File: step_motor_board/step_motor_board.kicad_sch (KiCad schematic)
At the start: 39 parts, among them J1 Prog (PinHeader_2x03_P2.54mm), J7 DebugUSART (PinHeader_01x03_P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, J8 Debug GPIO (PinHeader_01x02_P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, Q4 DTC114ECA (SOT-23), Q5 DTC114ECA (SOT-23), U1 ADM3485EARZ-REEL (SOIC-8), U3 STM32G070RBTx (LQFP-64), U5 AM1SS-2403SJZ, U9 PAI141M30 (SOIC-16)

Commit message: DC, contr, mb, step v2
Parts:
- removed J1: Prog (PinHeader_2x03_P2.54mm), Connector_PinHeader_2.54mm:PinHeader_2x03_P2.54mm_Vertical, symbol Connector_Generic:Conn_02x03_Odd_Even
- removed J7: DebugUSART (PinHeader_01x03_P2.54mm), Connector_PinHeader_2.54mm:PinHeader_1x03_P2.54mm_Vertical, symbol Connector:Conn_01x03_Pin
- removed J8: Debug GPIO (PinHeader_01x02_P2.54mm), Connector_PinHeader_2.54mm:PinHeader_1x02_P2.54mm_Vertical, symbol Connector:Conn_01x02_Pin
- added C42, C43: 20pF 50V 0603, Capacitor_SMD:C_0603_1608Metric, symbol Device:C
- added J1: PLL-10 (Prog), Connector_PinHeader_1.27mm:PinHeader_1x10_P1.27mm_Vertical, symbol Connector:Conn_01x10_Pin
- added TP20 (x11): TestPoint, PCM_4ms_TestPoint:TestPoint_D1, symbol Connector:TestPoint
- added Y1: Crystal_3225 8MHz, PCM_Crystal_AKL:Crystal_SMD_3225-4Pin_3.2x2.5mm, symbol Device:Crystal_GND24
- C14: value 47uF 63V D10,5 -> 47uF 63V D6,3 H11
- C3, C6, C7: value 0,1uF 50V 0805 -> 0,1uF 100V 0603; footprint PCM_Resistor_SMD_AKL:R_0805_2012Metric_Pad1.20x1.40mm_HandSolder -> Capacitor_SMD:C_0603_1608Metric_Pad1.08x0.95mm_HandSolder
- C4: footprint PCM_Resistor_SMD_AKL:R_0805_2012Metric_Pad1.20x1.40mm_HandSolder -> PCM_Capacitor_SMD_AKL:C_0805_2012Metric_Pad1.18x1.45mm_HandSolder
- C5, C8, C9: value 0,1uF 100V 0805 -> 0,1uF 100V 0603; footprint PCM_Capacitor_SMD_AKL:C_0805_2012Metric_Pad1.18x1.45mm_HandSolder -> Capacitor_SMD:C_0603_1608Metric_Pad1.08x0.95mm_HandSolder
- U9: value PAI141M30 (SOIC-16) -> Pai141M30 (SOIC-16)
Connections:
- net +24V: now also TP20.1
- net +3.3VRS485: now also TP20.1
- net +3V3: now also J1.1 (Pin_1)
- net GND1: now also TP20.1
- net GNDA: now also TP20.1
- net GNDD: now also C42.2, C43.2, J1.6 (Pin_6), TP20.1, Y1.2, Y1.4
- net GPIO1: now also J1.9 (Pin_9)
- net GPIO2: now also J1.10 (Pin_10)
- net NRST: now also J1.5 (Pin_5)
- net SWCLK: now also J1.3 (Pin_3)
- net SWDIO: now also J1.4 (Pin_4)
- net UART_RX: now also J1.8 (Pin_8)
- net UART_TX: now also J1.7 (Pin_7)
- net at R3.1, RS1.3 (Pin_3), RS1.8 (Pin_8)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: now also TP20.1
- net OSC_IN: now reaches U3.10 (PF0)
- net OSC_IN: now also C42.1, Y1.1
- net OSC_OUT: now reaches U3.11 (PF1)
- net OSC_OUT: now also C43.1, Y1.3
- net at R6.2, RS1.4 (Pin_4), RS1.7 (Pin_7)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: now also TP20.1
- net at R8.2, U1.2 (~{RE}), U1.3 (DE)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: now also TP20.1
- net at R1.1, U1.1 (RO), U9.11 (VID): now also TP20.1
- net at U1.4 (DI), U9.13 (VOB): now also TP20.1
- net at C12.1, L1.2, U5.2 (IN+): now also TP20.1
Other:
- moved on the sheet: C7, R1

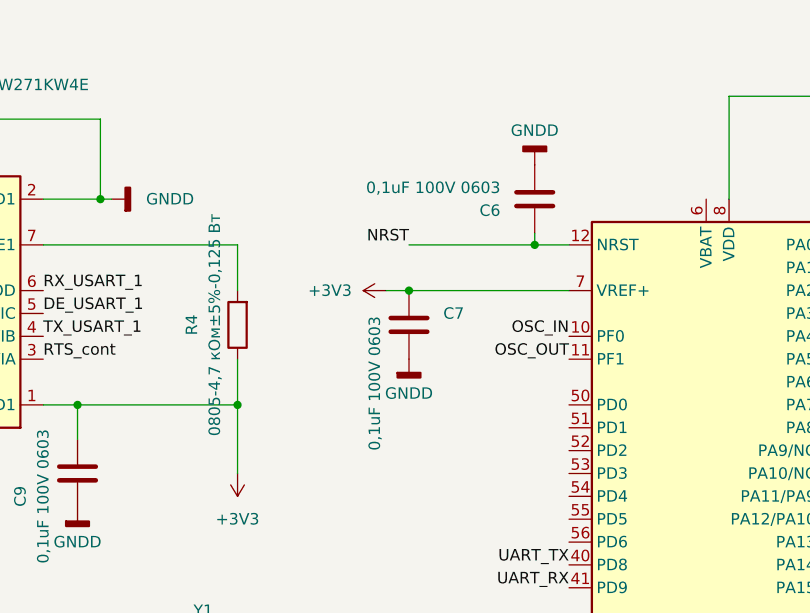
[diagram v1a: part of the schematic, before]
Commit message: Step  установлена бусинка
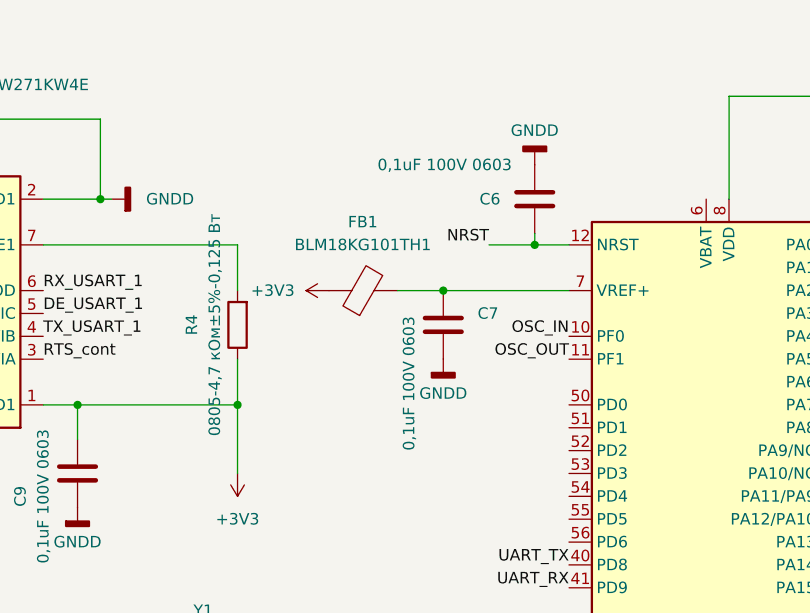
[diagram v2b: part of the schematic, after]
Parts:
- added FB1: BLM18KG101TH1, Inductor_SMD:L_0603_1608Metric, symbol Device:FerriteBead
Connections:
- net +3V3: now also FB1.1; no longer C7.1, U3.7 (VREF+)
- new net: C7.1, FB1.2, U3.7 (VREF+)
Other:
- moved on the sheet: C7

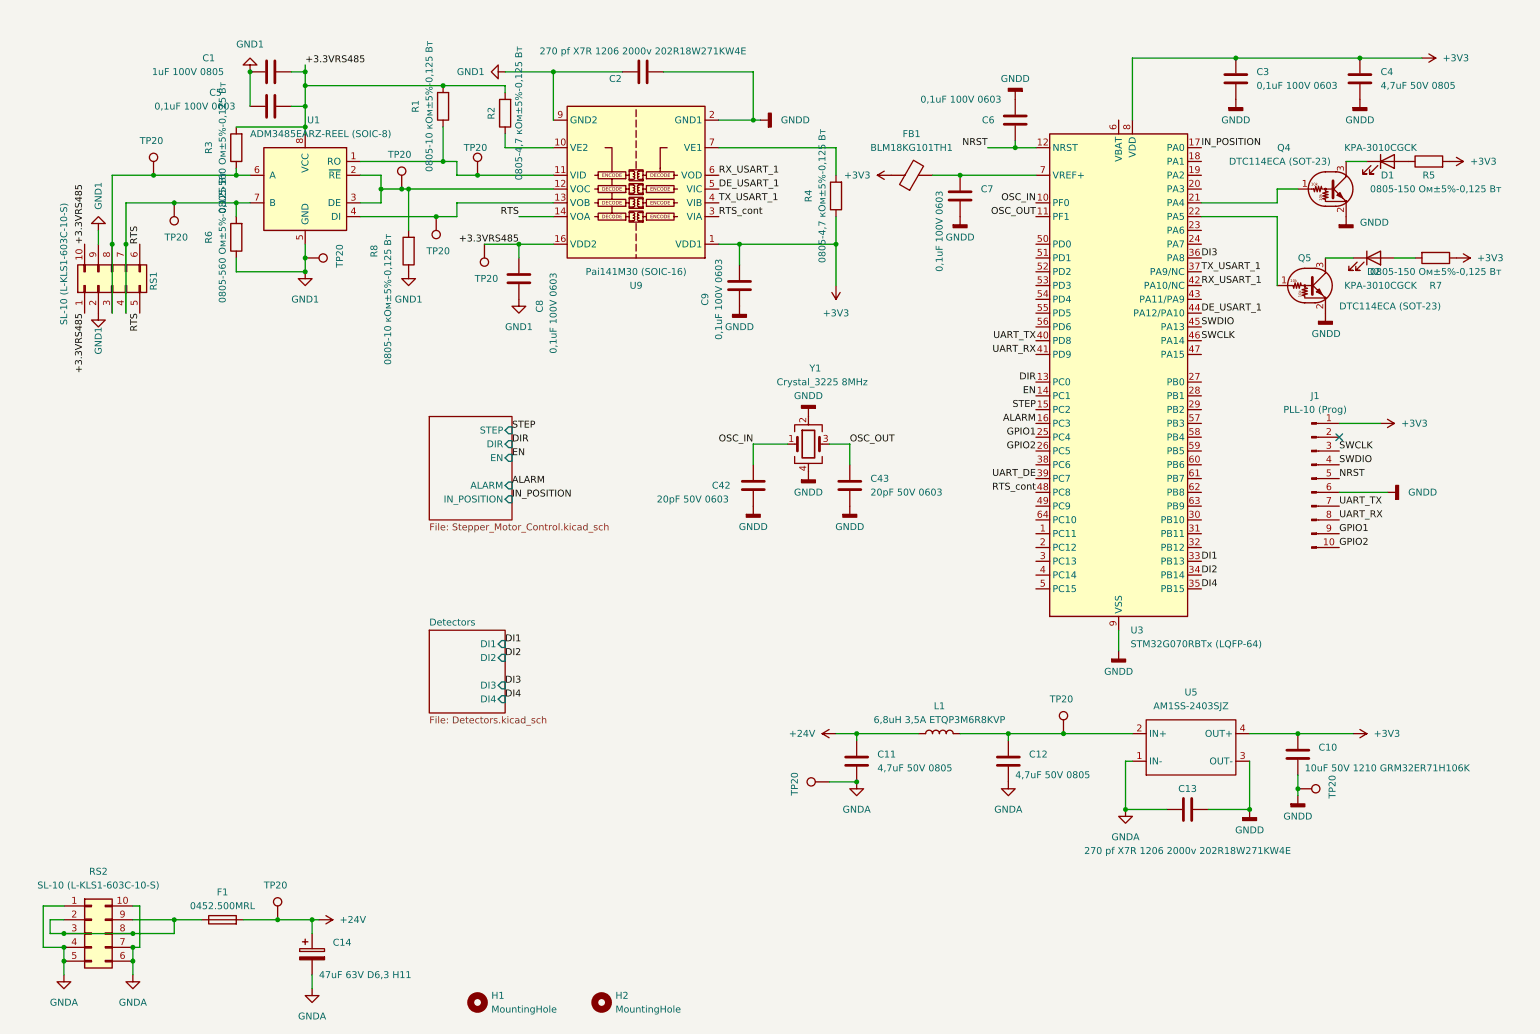
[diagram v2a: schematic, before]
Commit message: all замменил резисторы failsafe в плате контроллера и обрал из перечня во всех остальных
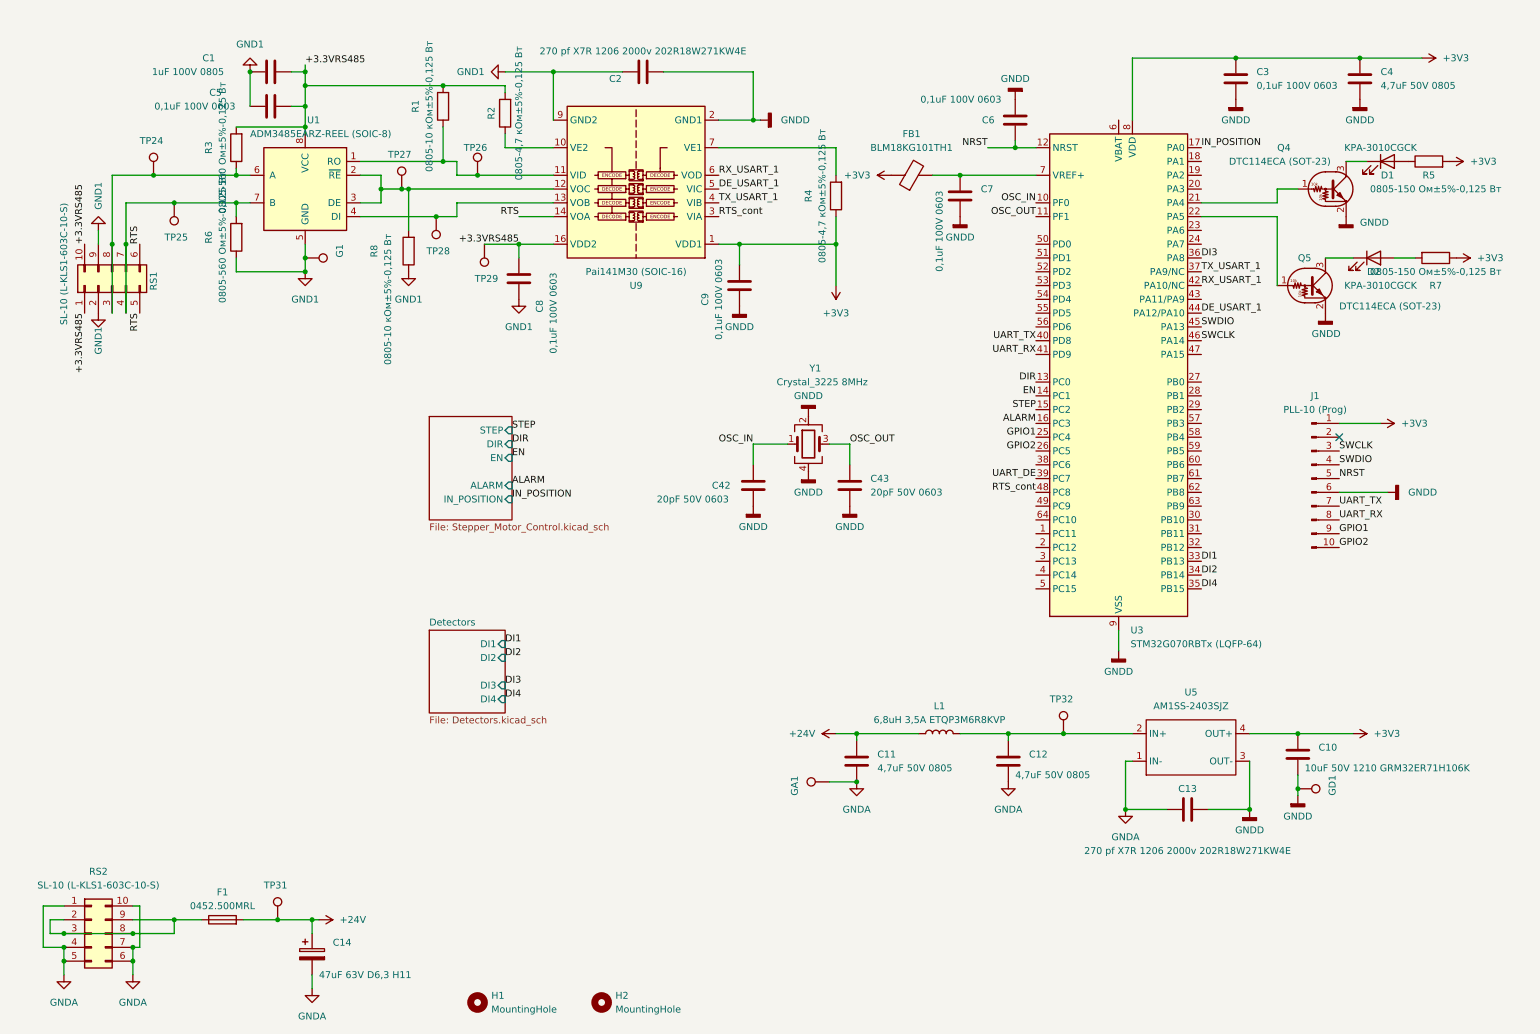
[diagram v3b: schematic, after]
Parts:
- C1, C11, C12, C4: footprint PCM_Capacitor_SMD_AKL:C_0805_2012Metric_Pad1.18x1.45mm_HandSolder -> Capacitor_SMD:C_0805_2012Metric
- C10: footprint PCM_Capacitor_SMD_AKL:C_1210_3225Metric_Pad1.42x2.65mm_HandSolder -> Capacitor_SMD:C_1210_3225Metric
- C13, C2: footprint PCM_Capacitor_SMD_Handsoldering_AKL:C_1210_3225Metric_Pad1.42x2.65mm -> Capacitor_SMD:C_1210_3225Metric
- C14: footprint PCM_Capacitor_THT_AKL:CP_Radial_D6.3mm_P2.50mm -> Capacitor_THT:CP_Radial_D6.3mm_P2.50mm
- C3, C5, C6, C7, C8, C9: footprint Capacitor_SMD:C_0603_1608Metric_Pad1.08x0.95mm_HandSolder -> Capacitor_SMD:C_0603_1608Metric
- F1: footprint PCM_Fuse_Handsoldering_AKL:Fuse_Littelfuse-NANO2-451_453 -> Fuse:Fuse_Littelfuse-NANO2-451_453
- G1, GA1, GD1, TP24, TP25, TP26, TP27, TP28, TP29, TP31, TP32: renamed from TP20; footprint PCM_4ms_TestPoint:TestPoint_D1 -> TestPoint:TestPoint_Pad_D1.0mm
- L1: footprint PCM_Inductor_SMD_Handsoldering_AKL:L_Bourns-SRN6028 -> Inductor_SMD:L_Bourns-SRN6028
- R1, R2, R4, R5, R7, R8: footprint PCM_4ms_Resistor:R_0805_2012Metric -> Resistor_SMD:R_0805_2012Metric
- R3, R6: footprint PCM_4ms_Resistor:R_0805_2012Metric -> Resistor_SMD:R_0805_2012Metric; now left out of the parts list
- Y1: footprint PCM_Crystal_AKL:Crystal_SMD_3225-4Pin_3.2x2.5mm -> Crystal:Crystal_SMD_3225-4Pin_3.2x2.5mm

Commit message: update schemas
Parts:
- C13, C2: value 270 pf X7R 1206 2000v 202R18W271KW4E -> 270 pf X7R 1206 2000v (202R18W271KW4E)
- F1: value 0452.500MRL -> 0451.500MRL
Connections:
- net DI1: now also U3.34 (PB14); no longer U3.33 (PB13)
- net DI2: now also U3.33 (PB13); no longer U3.34 (PB14)
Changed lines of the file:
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@@
 (kicad_sch
-	(version 20231120)
+	(version 20250114)
 	(generator "eeschema")
-	(generator_version "8.0")
+	(generator_version "9.0")
 	(paper "A4")
 	(junction
@@
 	(label "+3.3VRS485"
 		(at 22.86 50.8 90)
-		(fields_autoplaced yes)
 		(effects
 			(font
@@
 	(label "NRST"
 		(at 189.23 33.02 180)
-		(fields_autoplaced yes)
 		(effects
 			(font
@@
 		)
 	)
-	(label "DI1"
+	(label "DI2"
 		(at 228.6 109.22 0)
-		(fields_autoplaced yes)
 		(effects
 			(font
@@
 	(label "RTS_cont"
 		(at 139.7 45.72 0)
-		(fields_autoplaced yes)
 		(effects
 			(font
@@
 	(label "UART_TX"
 		(at 254 99.06 0)
-		(fields_autoplaced yes)
 		(effects
 			(font
@@
 	(label "UART_RX"
 		(at 254 101.6 0)
-		(fields_autoplaced yes)
 		(effects
 			(font
@@
 	(label "STEP"
 		(at 198.12 81.28 180)
-		(fields_autoplaced yes)
 		(effects
 			(font
@@
 	(label "IN_POSITION"
 		(at 101.6 97.79 0)
-		(fields_autoplaced yes)
 		(effects
 			(font
@@
 	(label "UART_TX"
 		(at 198.12 68.58 180)
-		(fields_autoplaced yes)
 		(effects
 			(font
@@
 	(label "RX_USART_1"
 		(at 228.6 58.42 0)
-		(fields_autoplaced yes)
 		(effects
 			(font
@@
 	(label "DIR"
 		(at 198.12 76.2 180)
-		(fields_autoplaced yes)
 		(effects
 			(font
@@
 	(label "UART_RX"
 		(at 198.12 71.12 180)
-		(fields_autoplaced yes)
 		(effects
 			(font
@@
 	(label "GPIO2"
 		(at 198.12 88.9 180)
-		(fields_autoplaced yes)
 		(effects
 			(font
@@
 	(label "ALARM"
 		(at 101.6 95.25 0)
-		(fields_autoplaced yes)
 		(effects
 			(font
@@
 	(label "UART_DE"
 		(at 198.12 93.98 180)
-		(fields_autoplaced yes)
 		(effects
 			(font
@@
 	(label "DE_USART_1"
 		(at 228.6 63.5 0)
-		(fields_autoplaced yes)
 		(effects
 			(font
@@
 	(label "OSC_OUT"
 		(at 163.83 87.63 0)
-		(fields_autoplaced yes)
 		(effects
 			(font
@@
 	(label "OSC_IN"
 		(at 198.12 43.18 180)
-		(fields_autoplaced yes)
 		(effects
 			(font
@@
 	(label "ALARM"
 		(at 198.12 83.82 180)
-		(fields_autoplaced yes)
 		(effects
 			(font
@@
 	(label "RTS_cont"
 		(at 198.12 96.52 180)
-		(fields_autoplaced yes)
 		(effects
 			(font
@@
 	(label "RTS"
 		(at 33.02 63.5 270)
-		(fields_autoplaced yes)
 		(effects
 			(font
@@
 	(label "RTS"
 		(at 33.02 50.8 90)
-		(fields_autoplaced yes)
 		(effects
 			(font
@@
 	(label "DIR"
 		(at 101.6 87.63 0)
-		(fields_autoplaced yes)
 		(effects
 			(font
@@
 	(label "GPIO1"
 		(at 254 104.14 0)
-		(fields_autoplaced yes)
 		(effects
 			(font
@@
 	(label "SWDIO"
 		(at 228.6 66.04 0)
-		(fields_autoplaced yes)
 		(effects
 			(font
@@
 	(label "SWCLK"
 		(at 254 88.9 0)
-		(fields_autoplaced yes)
 		(effects
 			(font
@@
 	(label "NRST"
 		(at 254 93.98 0)
-		(fields_autoplaced yes)
 		(effects
 			(font
@@
 	(label "DI4"
 		(at 100.33 134.62 0)
-		(fields_autoplaced yes)
 		(effects
 			(font
@@
 	(label "TX_USART_1"
 		(at 139.7 43.18 0)
-		(fields_autoplaced yes)
 		(effects
 			(font
@@
 	(label "DE_USART_1"
 		(at 139.7 40.64 0)
-		(fields_autoplaced yes)
 		(effects
 			(font
@@
 	(label "DI1"
 		(at 100.33 124.46 0)
-		(fields_autoplaced yes)
 		(effects
 			(font
@@
 	(label "+3.3VRS485"
 		(at 102.87 50.8 180)
-		(fields_autoplaced yes)
 		(effects
 			(font
@@
 	(label "GPIO1"
 		(at 198.12 86.36 180)
-		(fields_autoplaced yes)
 		(effects
 			(font
@@
 	(label "SWDIO"
 		(at 254 91.44 0)
-		(fields_autoplaced yes)
 		(effects
 			(font
@@
 	(label "DI3"
 		(at 100.33 132.08 0)
-		(fields_autoplaced yes)
 		(effects
 			(font
@@
 	(label "+3.3VRS485"
 		(at 22.86 63.5 270)
-		(fields_autoplaced yes)
 		(effects
 			(font
@@
 	(label "OSC_OUT"
 		(at 198.12 45.72 180)
-		(fields_autoplaced yes)
 		(effects
 			(font
@@
 	(label "DI4"
 		(at 228.6 114.3 0)
-		(fields_autoplaced yes)
 		(effects
 			(font
@@
 	(label "+3.3VRS485"
 		(at 63.5 17.78 0)
-		(fields_autoplaced yes)
 		(effects
 			(font
@@
 	(label "GPIO2"
 		(at 254 106.68 0)
-		(fields_autoplaced yes)
 		(effects
 			(font
@@
 	(label "TX_USART_1"
 		(at 228.6 55.88 0)
-		(fields_autoplaced yes)
 		(effects
 			(font
@@
 	(label "RTS"
 		(at 102.87 45.72 180)
-		(fields_autoplaced yes)
 		(effects
 			(font
@@
 	(label "DI2"
 		(at 100.33 127 0)
-		(fields_autoplaced yes)
 		(effects
 			(font
@@
 	(label "EN"
 		(at 101.6 90.17 0)
-		(fields_autoplaced yes)
 		(effects
 			(font
@@
 	(label "IN_POSITION"
 		(at 228.6 33.02 0)
-		(fields_autoplaced yes)
 		(effects
 			(font
@@
 	(label "RX_USART_1"
 		(at 139.7 38.1 0)
-		(fields_autoplaced yes)
 		(effects
 			(font
@@
 	(label "STEP"
 		(at 101.6 85.09 0)
-		(fields_autoplaced yes)
 		(effects
 			(font
@@
 	(label "SWCLK"
 		(at 228.6 68.58 0)
-		(fields_autoplaced yes)
 		(effects
 			(font
@@
 	(label "EN"
 		(at 198.12 78.74 180)
-		(fields_autoplaced yes)
 		(effects
 			(font
@@
 	(label "DI3"
 		(at 228.6 53.34 0)
-		(fields_autoplaced yes)
 		(effects
 			(font
@@
 	(label "OSC_IN"
 		(at 146.05 87.63 180)
-		(fields_autoplaced yes)
 		(effects
 			(font
@@
 		)
 	)
-	(label "DI2"
+	(label "DI1"
 		(at 228.6 111.76 0)
-		(fields_autoplaced yes)
 		(effects
 			(font
@@
 			)
 		)
-		(property "Value" "270 pf X7R 1206 2000v 202R18W271KW4E"
+		(property "Value" "270 pf X7R 1206 2000v (202R18W271KW4E)"
 			(at 226.06 162.56 90)
 			(effects
@@
 			)
 		)
-		(property "Value" "270 pf X7R 1206 2000v 202R18W271KW4E"
+		(property "Value" "270 pf X7R 1206 2000v (202R18W271KW4E)"
 			(at 125.73 15.24 90)
 			(effects
@@
 		(fields_autoplaced yes)
 		(property "Reference" "F1"
-			(at 48.26 170.18 90)
+			(at 48.26 168.91 90)
 			(effects
 				(font
@@
 			)
 		)
-		(property "Value" "0452.500MRL"
-			(at 48.26 172.72 90)
+		(property "Value" "0451.500MRL"
+			(at 48.26 171.45 90)
 			(effects
 				(font
@@
 		(at 86.36 82.55)
 		(size 15.24 19.05)
+		(exclude_from_sim no)
+		(in_bom yes)
+		(on_board yes)
+		(dnp no)
 		(fields_autoplaced yes)
 		(stroke
@@
 		(at 86.36 121.92)
 		(size 13.97 15.24)
+		(exclude_from_sim no)
+		(in_bom yes)
+		(on_board yes)
+		(dnp no)
 		(fields_autoplaced yes)
 		(stroke
@@
 		)
 	)
+	(embedded_fonts no)
 )
